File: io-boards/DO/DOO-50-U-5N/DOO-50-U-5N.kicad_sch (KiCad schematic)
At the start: 2 parts, among them J1 GPP_Conn_01x12_Pin, U1 PC817

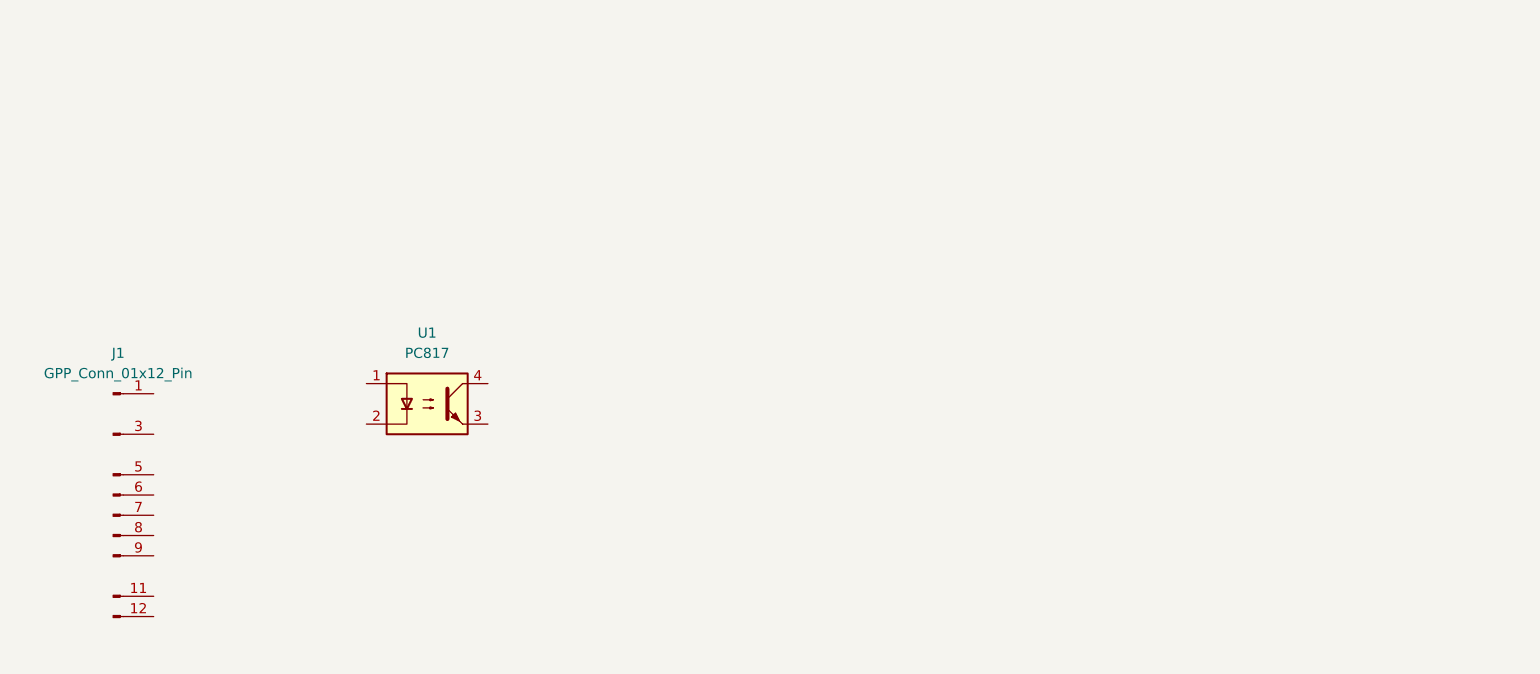
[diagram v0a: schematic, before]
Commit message: New DO added.
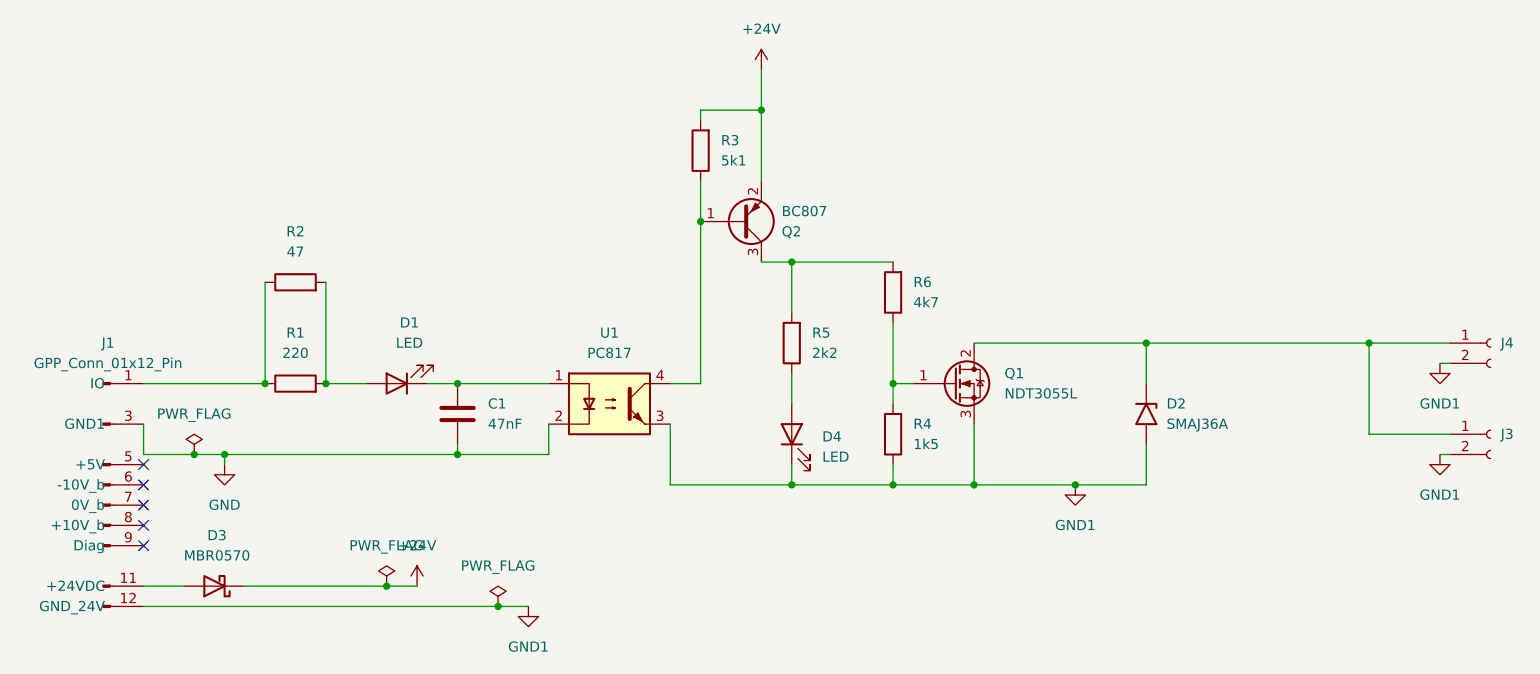
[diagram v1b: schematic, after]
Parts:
- added C1: 47nF, Capacitor_SMD:C_0201_0603Metric, symbol Device:C
- added D1, D4: LED, LED_SMD:LED_0402_1005Metric_Pad0.77x0.64mm_HandSolder, symbol Device:LED
- added D2: SMAJ36A, Diode_SMD:D_SMA, symbol Diode:SMAJ36A
- added D3: MBR0570, Diode_SMD:D_SOD-123, symbol Diode:MBR0570
- added J3: Conn_01x02_Socket, tuxmio:KF141x_SMD, symbol Connector:Conn_01x02_Socket
- added J4: Conn_01x02_Socket, Connector_PinSocket_2.54mm:PinSocket_1x02_P2.54mm_Horizontal, symbol Connector:Conn_01x02_Socket
- added Q1: NDT3055L, Package_TO_SOT_SMD:SOT-223-3_TabPin2, symbol Transistor_FET:NDT3055L
- added Q2: BC807, Package_TO_SOT_SMD:SOT-23, symbol Transistor_BJT:BC807
- added R1: 220, Resistor_SMD:R_0402_1005Metric_Pad0.72x0.64mm_HandSolder, symbol Device:R
- added R2: 47, Resistor_SMD:R_0402_1005Metric_Pad0.72x0.64mm_HandSolder, symbol Device:R
- added R3: 5k1, Resistor_SMD:R_0402_1005Metric_Pad0.72x0.64mm_HandSolder, symbol Device:R
- added R4: 1k5, Resistor_SMD:R_0402_1005Metric_Pad0.72x0.64mm_HandSolder, symbol Device:R
- added R5: 2k2, Resistor_SMD:R_0402_1005Metric_Pad0.72x0.64mm_HandSolder, symbol Device:R
- added R6: 4k7, Resistor_SMD:R_0402_1005Metric_Pad0.72x0.64mm_HandSolder, symbol Device:R
- J1: footprint tuxmio:IO_GPP_connector_PinHeader_1x12_P2.54mm_Horizontal -> tuxmio:IO_GPP_PinHeader_1x12_P2.54mm_Horizontal
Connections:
- net at J1.1 (IO): now also R1.1, R2.1
- net at J1.11 (+24VDC): now also D3.2 (A)
- net GND1: now reaches J1.12 (GND_24V)
- net GND1: now also U1.3, D2.2 (A2), D4.1 (K), J3.2 (Pin_2), J4.2 (Pin_2), Q1.3 (S), R4.1
- net GND: now reaches J1.3 (GND1)
- net GND: now also U1.2, C1.2
- net at U1.1: now also C1.1, D1.1 (K)
- net at U1.4: now also Q2.1 (B), R3.1
- new net: D2.1 (A1), J3.1 (Pin_1), J4.1 (Pin_1), Q1.2 (D)
- new net: D1.2 (A), R1.2, R2.2
- new net: Q1.1 (G), R4.2, R6.1
- new net: D4.2 (A), R5.1
- new net: Q2.3 (C), R5.2, R6.2
- new net +24V: D3.1 (K), Q2.2 (E), R3.2
- no-connect marks 0 -> 5
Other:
- moved on the sheet: U1

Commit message: Made some corrections after assembling of prototype PCBs
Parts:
- added D5: SM4007, Diode_SMD:D_MELF_Handsoldering, symbol Diode:SM4007
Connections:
- net at D2.1 (A1), J3.1 (Pin_1), J4.1 (Pin_1)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: now also D5.2 (A)
- net fly: now reaches D3.2 (A), J1.11 (+24VDC)
- net fly: now also D5.1 (K)
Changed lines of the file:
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@@
+	)
+	(junction
+		(at 241.3 96.52)
+		(diameter 0)
+		(color 0 0 0 0)
 	)
 	(junction
@@
 	)
 	(junction
+		(at 128.27 127)
+		(diameter 0)
+		(color 0 0 0 0)
+	)
+	(junction
 		(at 207.01 114.3)
 		(diameter 0)
@@
 	(wire
 		(pts
+			(xy 128.27 125.73) (xy 128.27 127)
+		)
+		(stroke
+			(width 0)
+			(type default)
+		)
+	)
+	(wire
+		(pts
 			(xy 148.59 101.6) (xy 148.59 88.9)
 		)
@@
 	(wire
 		(pts
-			(xy 125.73 127) (xy 130.81 127)
+			(xy 125.73 127) (xy 128.27 127)
 		)
 		(stroke
@@
 	(wire
 		(pts
+			(xy 241.3 62.23) (xy 241.3 74.93)
+		)
+		(stroke
+			(width 0)
+			(type default)
+		)
+	)
+	(wire
+		(pts
 			(xy 251.46 96.52) (xy 251.46 101.6)
 		)
@@
 	(wire
 		(pts
+			(xy 241.3 96.52) (xy 251.46 96.52)
+		)
+		(stroke
+			(width 0)
+			(type default)
+		)
+	)
+	(wire
+		(pts
 			(xy 195.58 76.2) (xy 195.58 81.28)
 		)
@@
 	(wire
 		(pts
-			(xy 229.87 96.52) (xy 251.46 96.52)
+			(xy 229.87 96.52) (xy 241.3 96.52)
 		)
 		(stroke
@@
 	(wire
 		(pts
+			(xy 128.27 127) (xy 130.81 127)
+		)
+		(stroke
+			(width 0)
+			(type default)
+		)
+	)
+	(wire
+		(pts
 			(xy 203.2 62.23) (xy 203.2 67.31)
 		)
@@
 			(width 0)
 			(type default)
+		)
+	)
+	(wire
+		(pts
+			(xy 241.3 82.55) (xy 241.3 96.52)
+		)
+		(stroke
+			(width 0)
+			(type default)
+		)
+	)
+	(global_label "fly"
+		(shape input)
+		(at 128.27 125.73 90)
+		(fields_autoplaced yes)
+		(effects
+			(font
+				(size 1.27 1.27)
+			)
+			(justify left)
+		)
+		(property "Intersheetrefs" "${INTERSHEET_REFS}"
+			(at 128.27 120.3863 90)
+			(effects
+				(font
+					(size 1.27 1.27)
+				)
+				(justify left)
+				(hide yes)
+			)
+		)
+	)
+	(global_label "fly"
+		(shape input)
+		(at 241.3 62.23 90)
+		(fields_autoplaced yes)
+		(effects
+			(font
+				(size 1.27 1.27)
+			)
+			(justify left)
+		)
+		(property "Intersheetrefs" "${INTERSHEET_REFS}"
+			(at 241.3 56.8863 90)
+			(effects
+				(font
+					(size 1.27 1.27)
+				)
+				(justify left)
+				(hide yes)
+			)
 		)
 	)
@@
 					(unit 1)
 				)
+			)
+		)
+	)
+	(symbol
+		(lib_id "Diode:SM4007")
+		(at 241.3 78.74 270)
+		(unit 1)
+		(exclude_from_sim no)
+		(in_bom yes)
+		(on_board yes)
+		(dnp no)
+		(fields_autoplaced yes)
+		(property "Reference" "D5"
+			(at 243.84 77.4699 90)
+			(effects
+				(font
+					(size 1.27 1.27)
+				)
+				(justify left)
+			)
+		)
+		(property "Value" "SM4007"
+			(at 243.84 80.0099 90)
+			(effects
+				(font
+					(size 1.27 1.27)
+				)
+				(justify left)
+			)
+		)
+		(property "Footprint" "Diode_SMD:D_MELF_Handsoldering"
+			(at 236.855 78.74 0)
+			(effects
+				(font
+					(size 1.27 1.27)
+				)
+				(hide yes)
+			)
+		)
+		(property "Datasheet" "http://cdn-reichelt.de/documents/datenblatt/A400/SMD1N400%23DIO.pdf"
+			(at 241.3 78.74 0)
+			(effects
+				(font
+					(size 1.27 1.27)
+				)
+				(hide yes)
+			)
+		)
+		(property "Description" "1000V 1A General Purpose Rectifier Diode, MELF"
+			(at 241.3 78.74 0)
+			(effects
+				(font
+					(size 1.27 1.27)
+				)
+				(hide yes)
+			)
+		)
+		(property "Sim.Device" "D"
+			(at 241.3 78.74 0)
+			(effects
+				(font
+					(size 1.27 1.27)
+				)
+				(hide yes)
+			)
+		)
+		(property "Sim.Pins" "1=K 2=A"
+			(at 241.3 78.74 0)
+			(effects
+				(font
+					(size 1.27 1.27)
+				)
+				(hide yes)
+			)
+		)
+		(pin "1"
+		)
+		(pin "2"
+		)
+		(instances
+			(project ""
+				(path "/30fdd7bc-1110-4c31-98f3-91e8c10b2a68"
+					(reference "D5")
+					(unit 1)
+				)
